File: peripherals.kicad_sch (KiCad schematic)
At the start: 35 parts, among them J8 Conn_01x04_MountingPin, U1 MIMX8MM6DVTLZAA, U30 TCA9803, U31 74LVC2G07

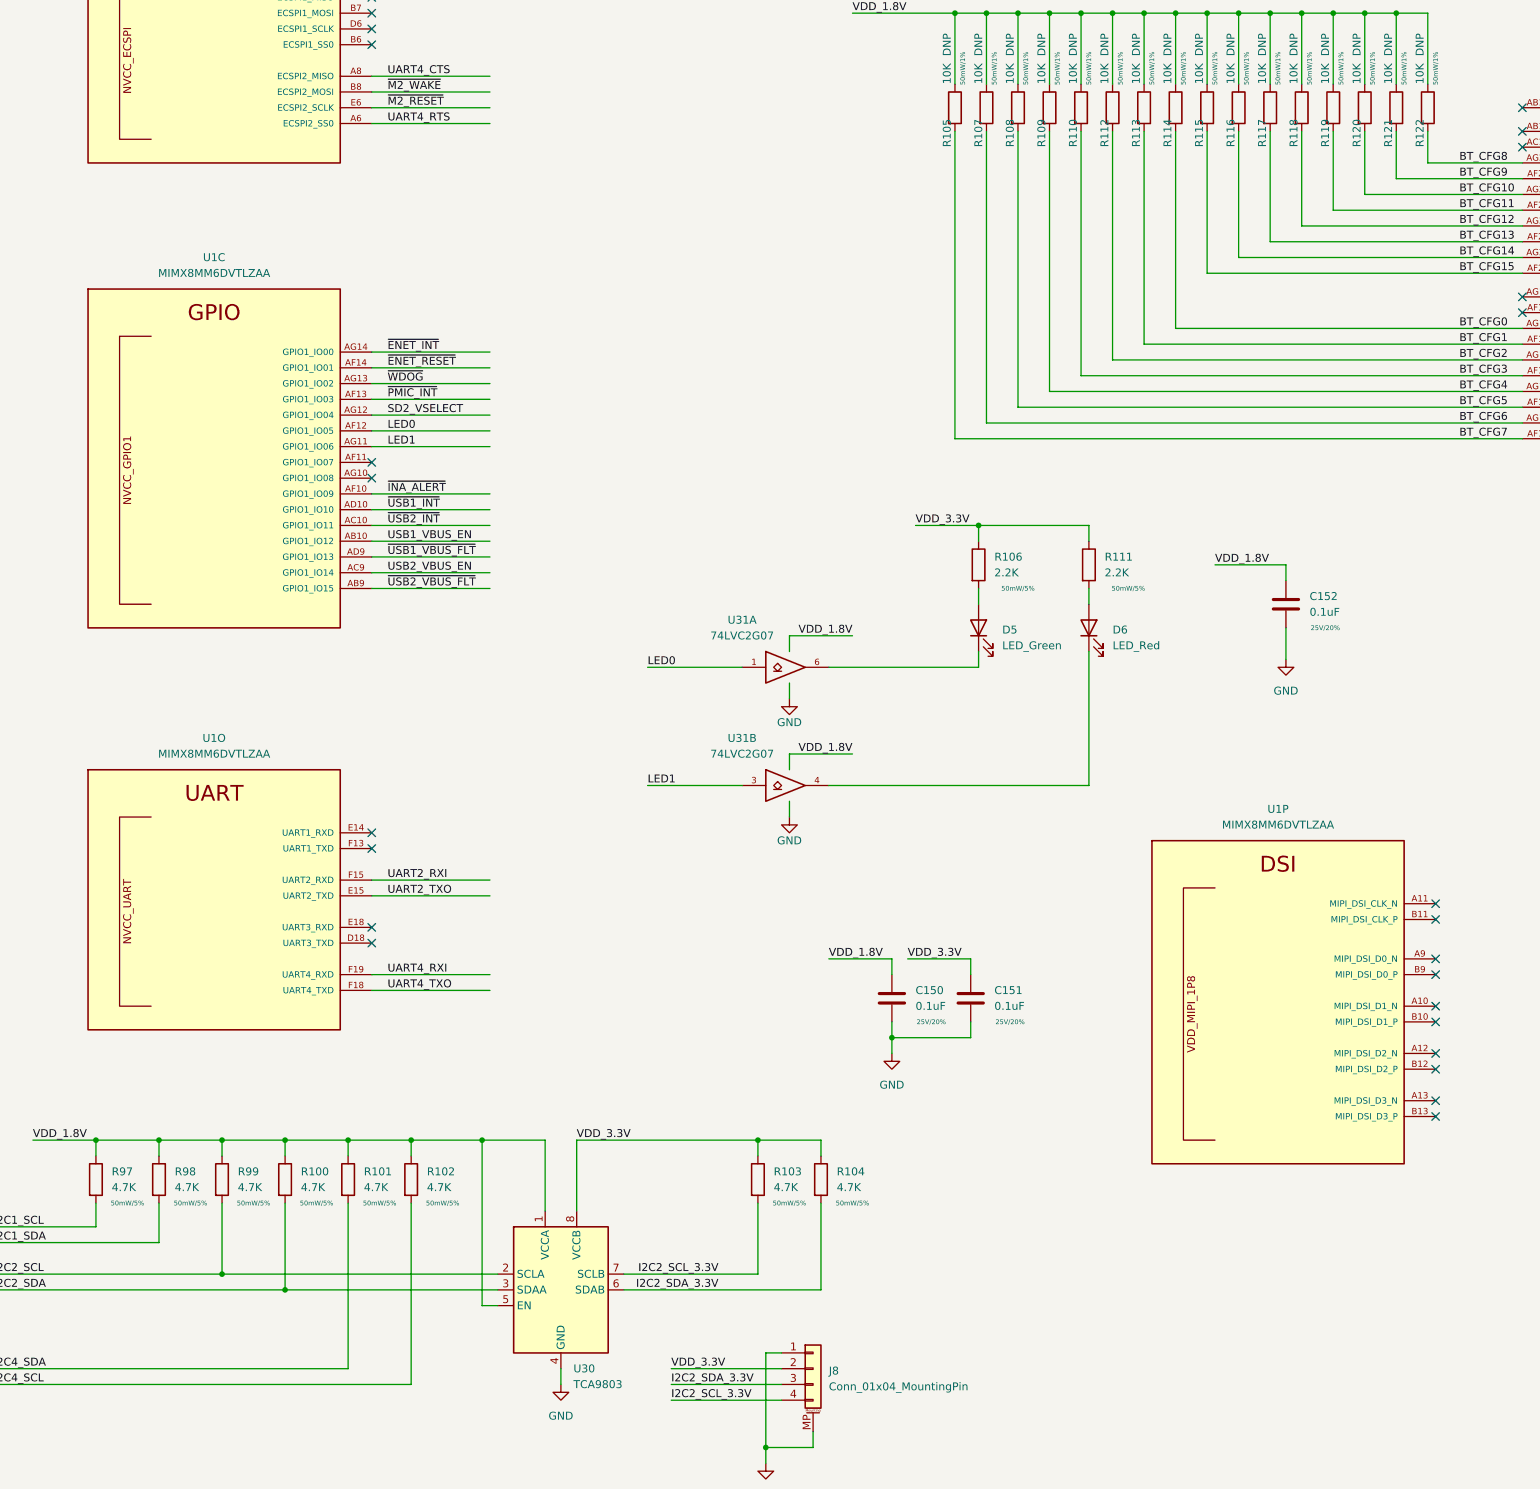
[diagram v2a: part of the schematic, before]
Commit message: inital routing of ddr data bus, sch work
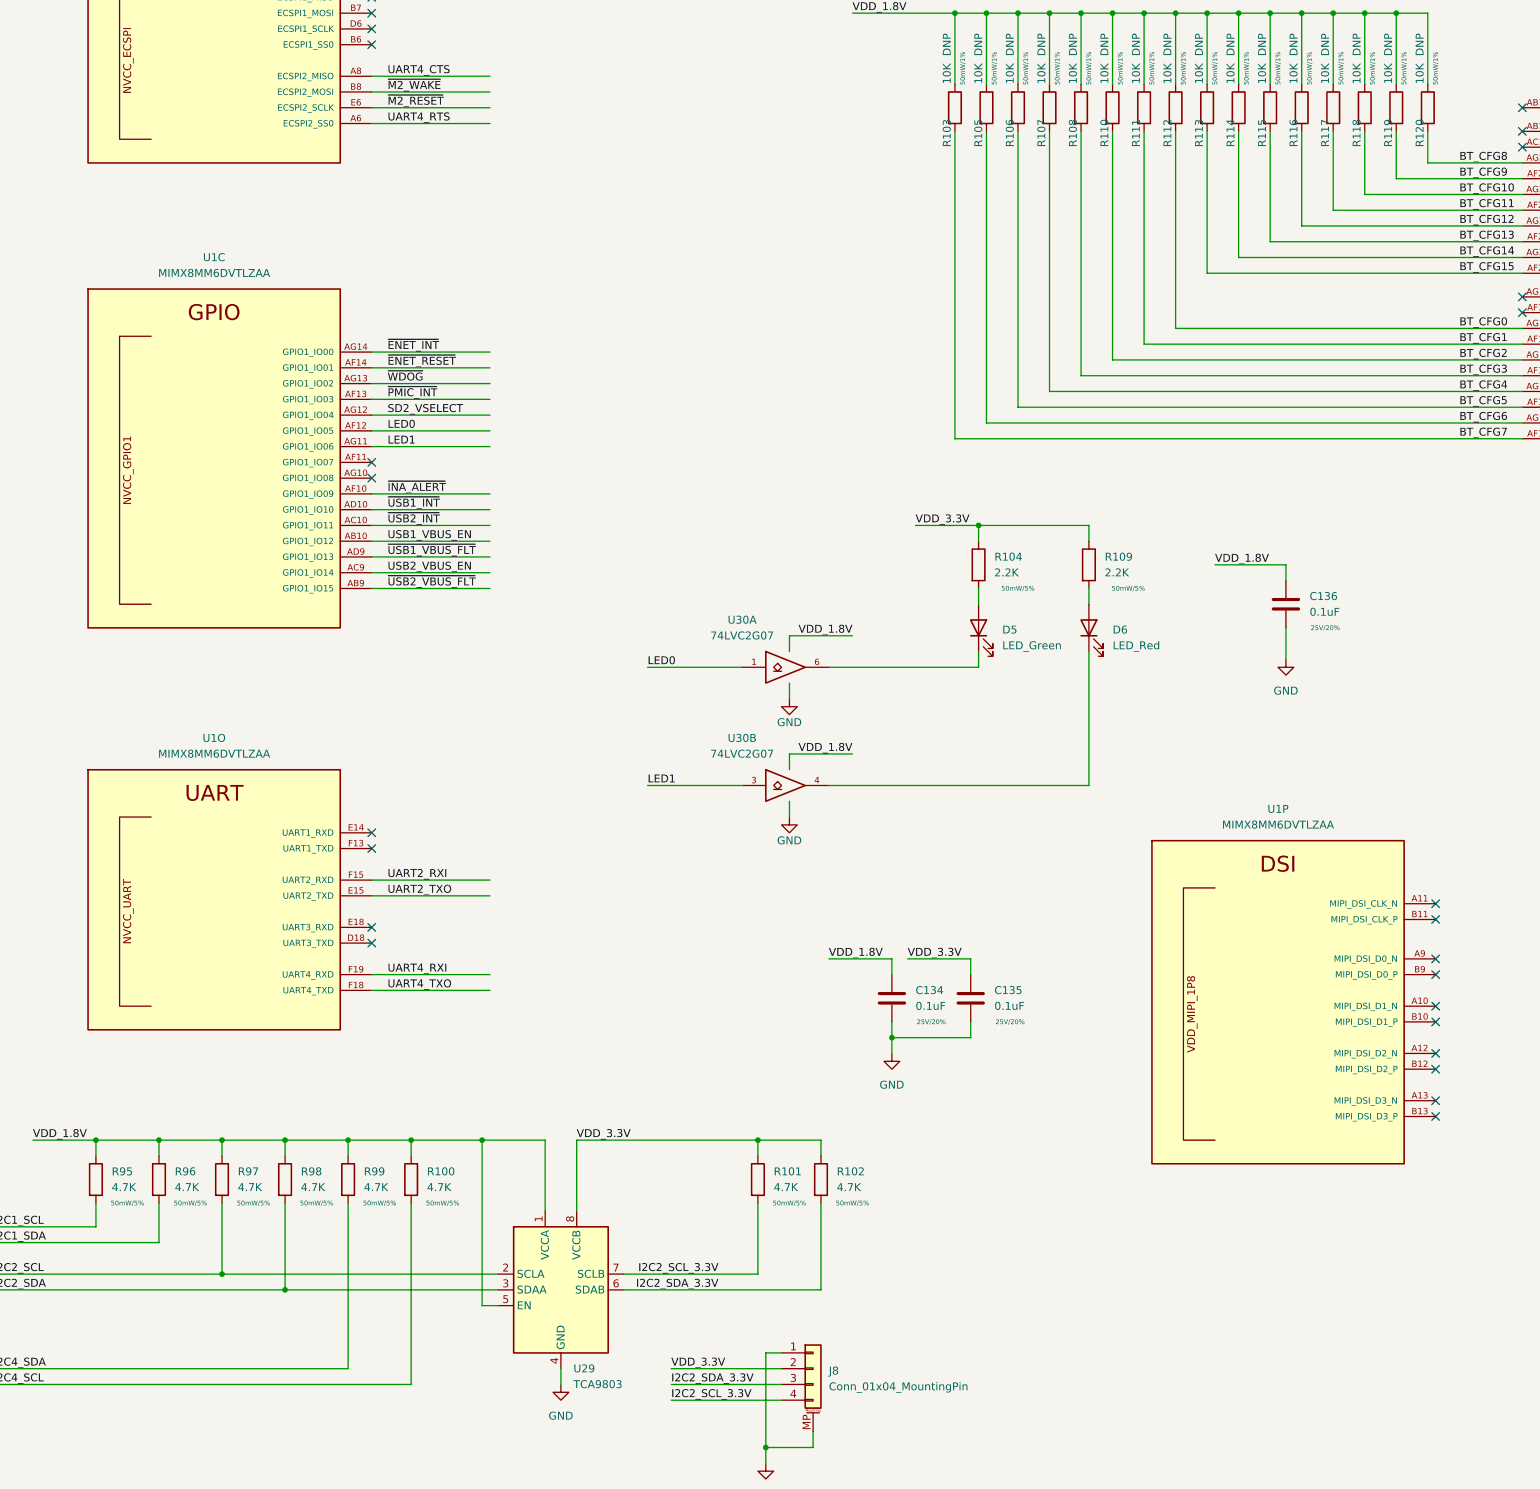
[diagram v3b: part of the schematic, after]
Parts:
- renumbered C150 to C134, C151 to C135, C152 to C136, R102 to R100, R103 to R101, R104 to R102, R105 to R103, R106 to R104, R107 to R105, R108 to R106, R109 to R107, R110 to R108, R111 to R109, R112 to R110, R113 to R111, R114 to R112, R115 to R113, R116 to R114, R117 to R115, R118 to R116, R119 to R117, R120 to R118, R121 to R119, R122 to R120, R97 to R95, R98 to R96, R99 to R97, R100 to R98, R101 to R99, U30 to U29, U31 to U30

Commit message: add SN65DSI86 DSI2DP ic, SCH, PCB work, flytime work
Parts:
- removed unit 16 of U1
- removed unit 4 of U1
- added R104, R105: 4.7K, Resistor_SMD:R_0402_1005Metric, symbol Device:R
- renumbered C136 to C143, C134 to C144, C135 to C145, R95 to R100, R96 to R101, R97 to R102, R98 to R103, R99 to R106, R103 to R107, R105 to R108, R100 to R109, R104 to R110, R106 to R111, R107 to R112, R108 to R113, R110 to R114, R109 to R115, R111 to R116, R112 to R117, R113 to R118, R114 to R119, R115 to R120, R116 to R121, R117 to R122, R101 to R123, R118 to R124, R119 to R125, R102 to R126, R120 to R127, U29 to U31
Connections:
- net I2C4_SCL: now also R106.2, U1.D13 (I2C4_SCL); no longer R109.2, U1.E13 (I2C4_SDA)
- net I2C4_SDA: now also R109.2, U1.E13 (I2C4_SDA); no longer R106.2, U1.D13 (I2C4_SCL)
- net VCC: now also R104.1, R105.1
- net ~{DSI86_EN}: now reaches U1.A7 (ECSPI1_MISO)
- net DSI86_INT: now reaches U1.B7 (ECSPI1_MOSI)
- net I2C3_SCL: now reaches U1.E10 (I2C3_SCL)
- net I2C3_SCL: now also R104.2
- net I2C3_SDA: now reaches U1.F10 (I2C3_SDA)
- net I2C3_SDA: now also R105.2
- no-connect marks 49 -> 35
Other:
- moved on the sheet: C143, D5, D6, J8, R106, R107, R108, R109, R110, R111, R112, R113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

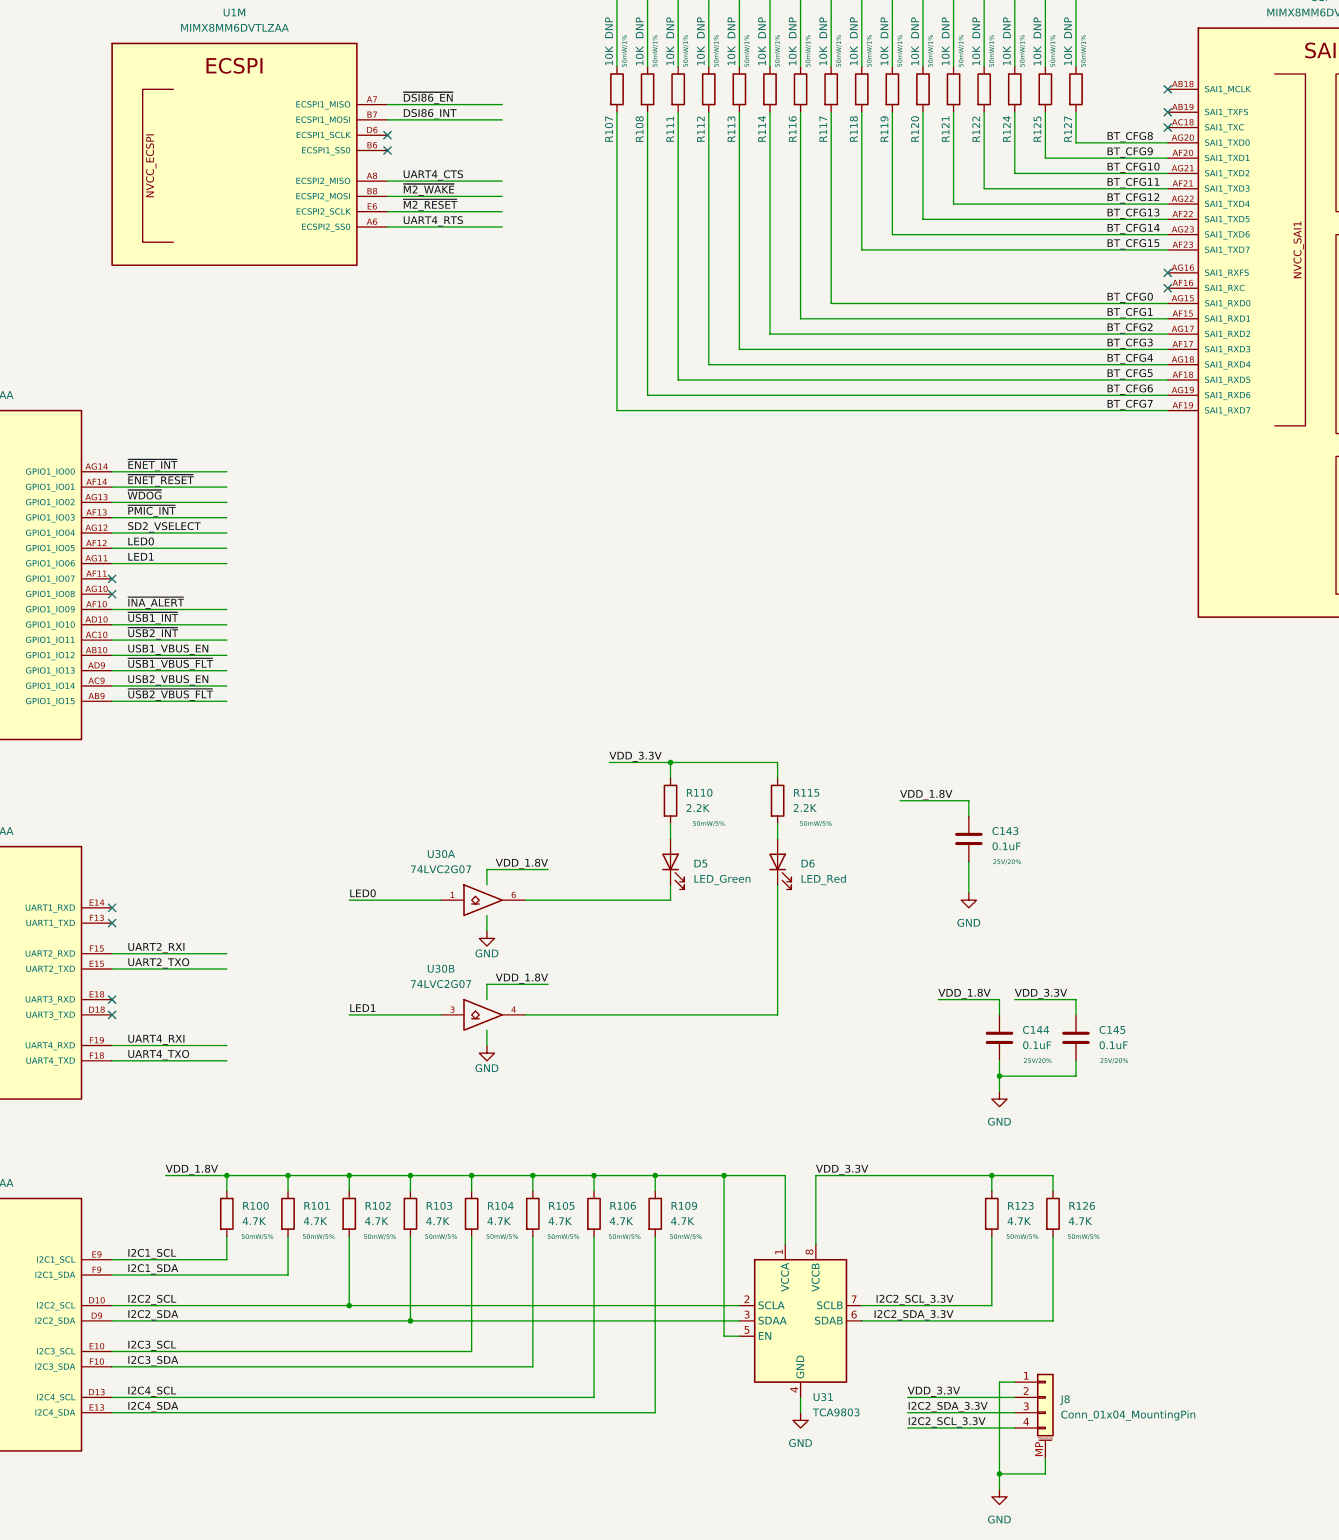
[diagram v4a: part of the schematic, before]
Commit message: add UART4 connector
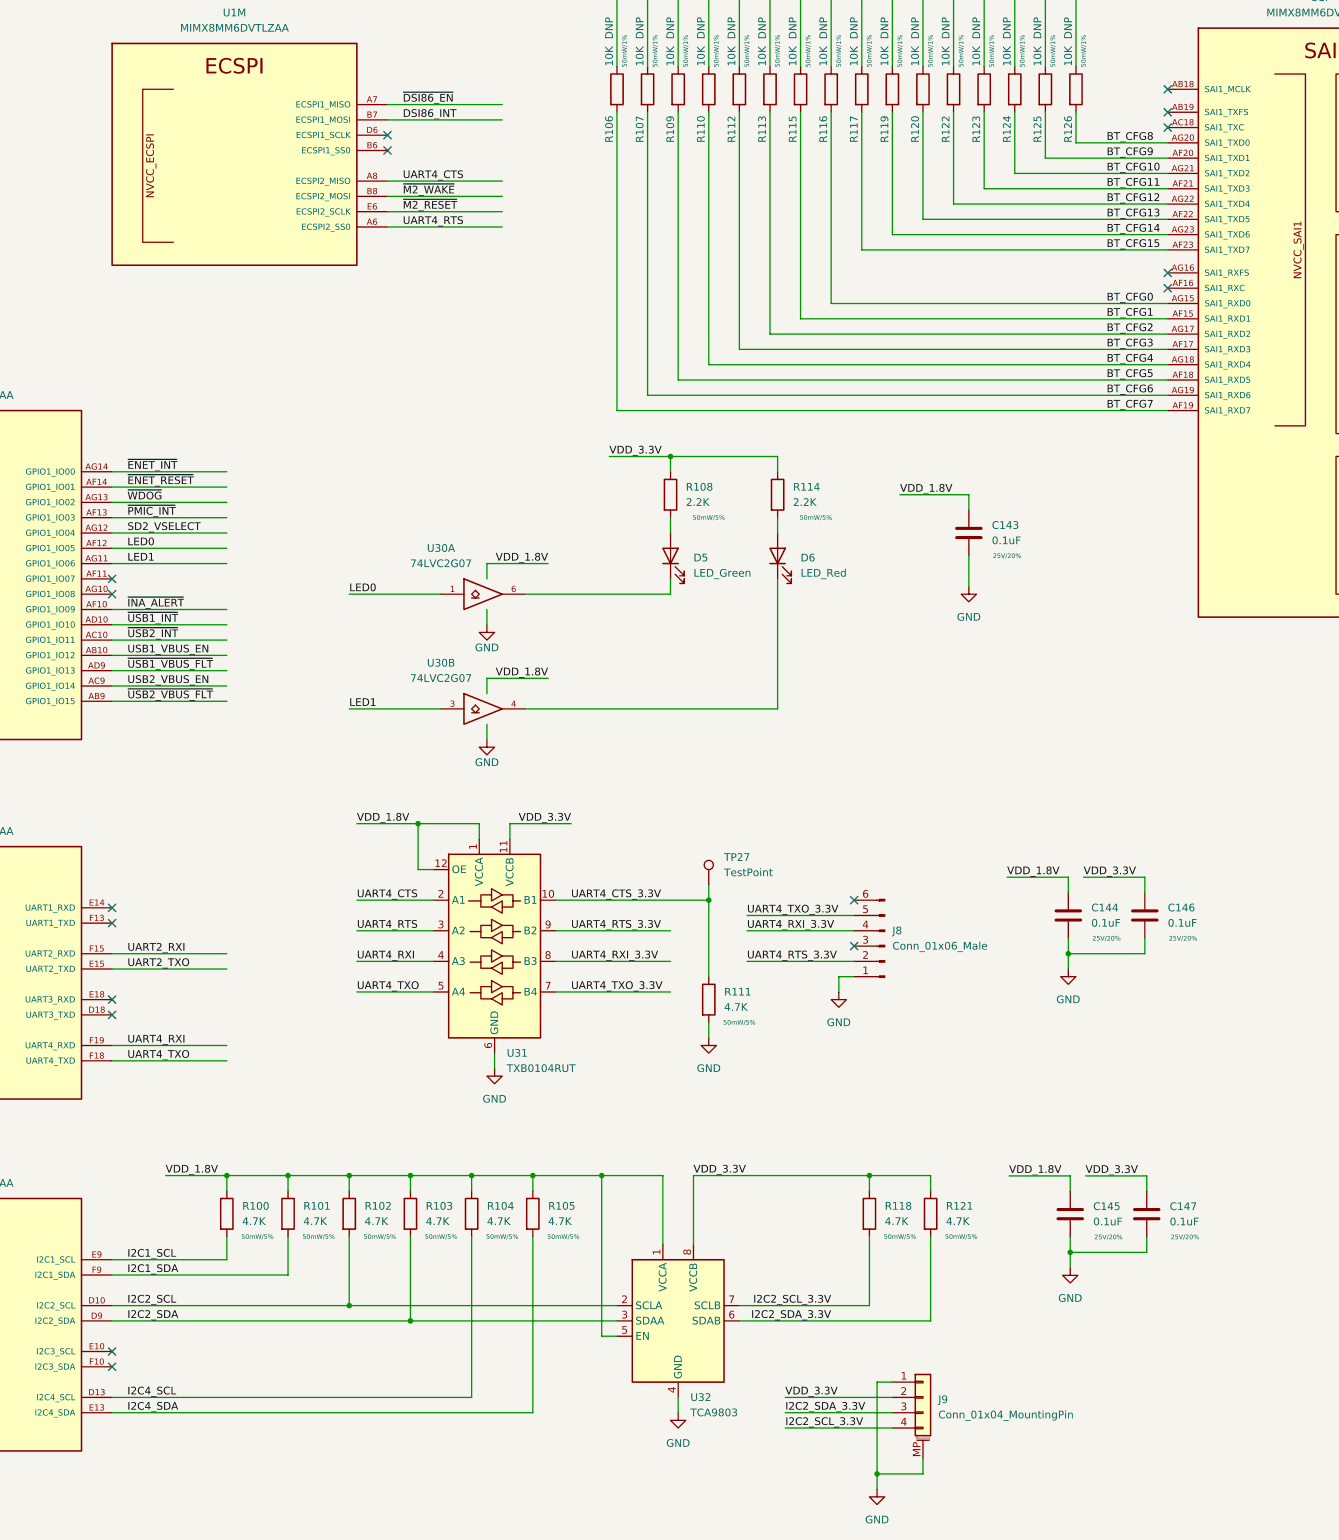
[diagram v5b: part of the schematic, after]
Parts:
- removed R104, R105: 4.7K, Resistor_SMD:R_0402_1005Metric, symbol Device:R
- added C144, C146: 0.1uF, Capacitor_SMD:C_0402_1005Metric, symbol Device:C
- added J8: Conn_01x06_Male, Connector_Harwin:Harwin_M20-89006xx_1x06_P2.54mm_Horizontal, symbol Connector:Conn_01x06_Male
- added R111: 4.7K, Resistor_SMD:R_0402_1005Metric, symbol Device:R
- added TP27: TestPoint, TestPoint:TestPoint_Pad_D1.0mm, symbol Connector:TestPoint
- added U31: TXB0104RUT, Package_DFN_QFN:Texas_R_PUQFN-N12, symbol Logic_LevelTranslator:TXB0104RUT
- renumbered C144 to C145, C145 to C147, J8 to J9, R106 to R104, R109 to R105, R107 to R106, R108 to R107, R110 to R108, R111 to R109, R112 to R110, R113 to R112, R114 to R113, R115 to R114, R116 to R115, R117 to R116, R118 to R117, R123 to R118, R126 to R121, R121 to R122, R122 to R123, R127 to R126, U31 to U32
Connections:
- net GND: now also C144.2, C146.2, J8.1 (Pin_1), R111.2, U31.6 (GND)
- net UART4_CTS: now also U31.2 (A1)
- net UART4_RTS: now also U31.3 (A2)
- net UART4_RXI: now also U31.4 (A3)
- net UART4_TXO: now also U31.5 (A4)
- net VCC: now also C144.1, U31.1 (VCCA), U31.12 (OE)
- net VDD_3.3V: now also C146.1, U31.11 (VCCB)
- net I2C3_SCL: no longer names the net of U1.E10 (I2C3_SCL)
- net I2C3_SDA: no longer names the net of U1.F10 (I2C3_SDA)
- new net UART4_CTS_3.3V: R111.1, TP27.1, U31.10 (B1)
- new net UART4_RTS_3.3V: J8.2 (Pin_2), U31.9 (B2)
- new net UART4_RXI_3.3V: J8.4 (Pin_4), U31.8 (B3)
- new net UART4_TXO_3.3V: J8.5 (Pin_5), U31.7 (B4)
- no-connect marks 35 -> 39
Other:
- moved on the sheet: C143, C145, C147, D5, D6, J9, R104, R105, R108, R114, R118, R121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
